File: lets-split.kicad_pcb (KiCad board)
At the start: 2 copper layers, 124 x 85.9 mm, 60 parts, among them J1 USB_C_Receptacle_USB2.0, SW1 Key_Tab, SW10 Key_D, SW11 Key_F, SW12 Key_G, SW13 Key_Shift, SW14 Key_Z, SW15 Key_X, SW16 Key_C, SW17 Key_V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

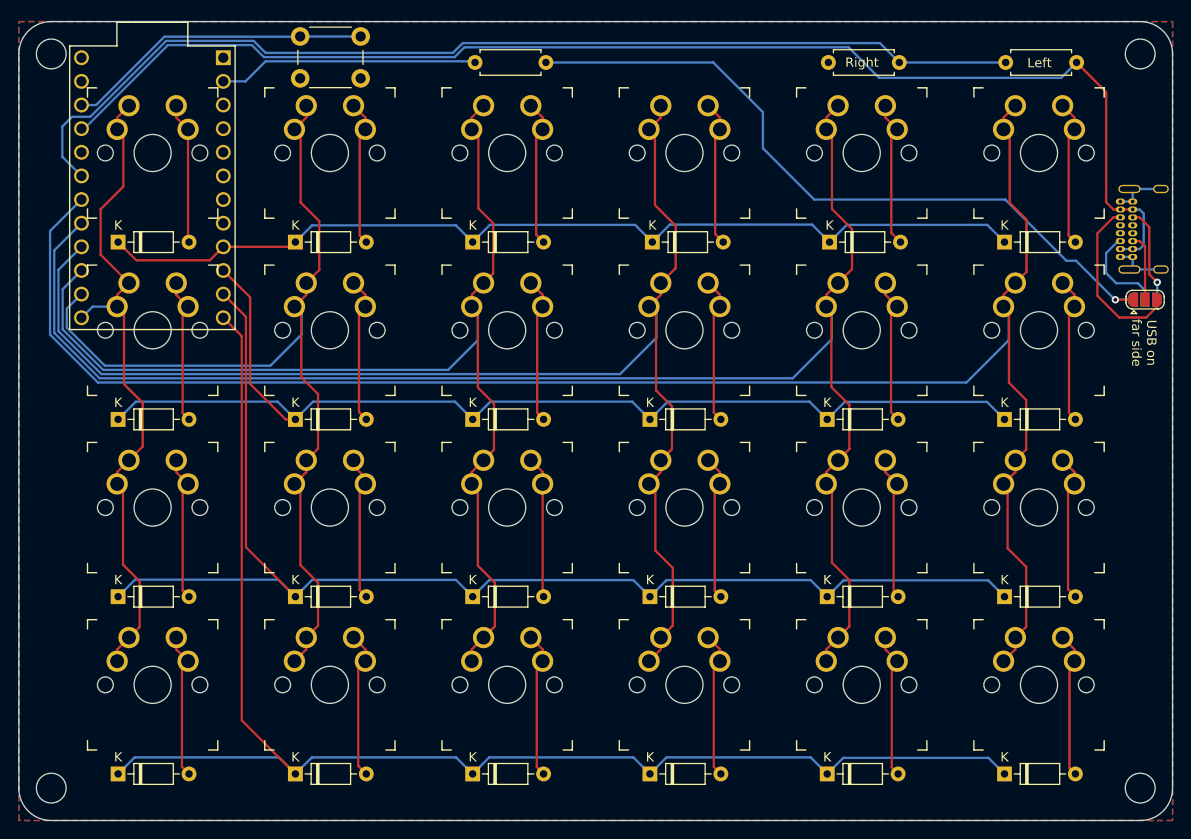
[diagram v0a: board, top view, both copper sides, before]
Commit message: Revised board
Moved controller over 1 column
moved usb-c to top edge
simplified routing overall

now only 1 via, and absolute minimum number of traces under the USB jack
(one each side!)
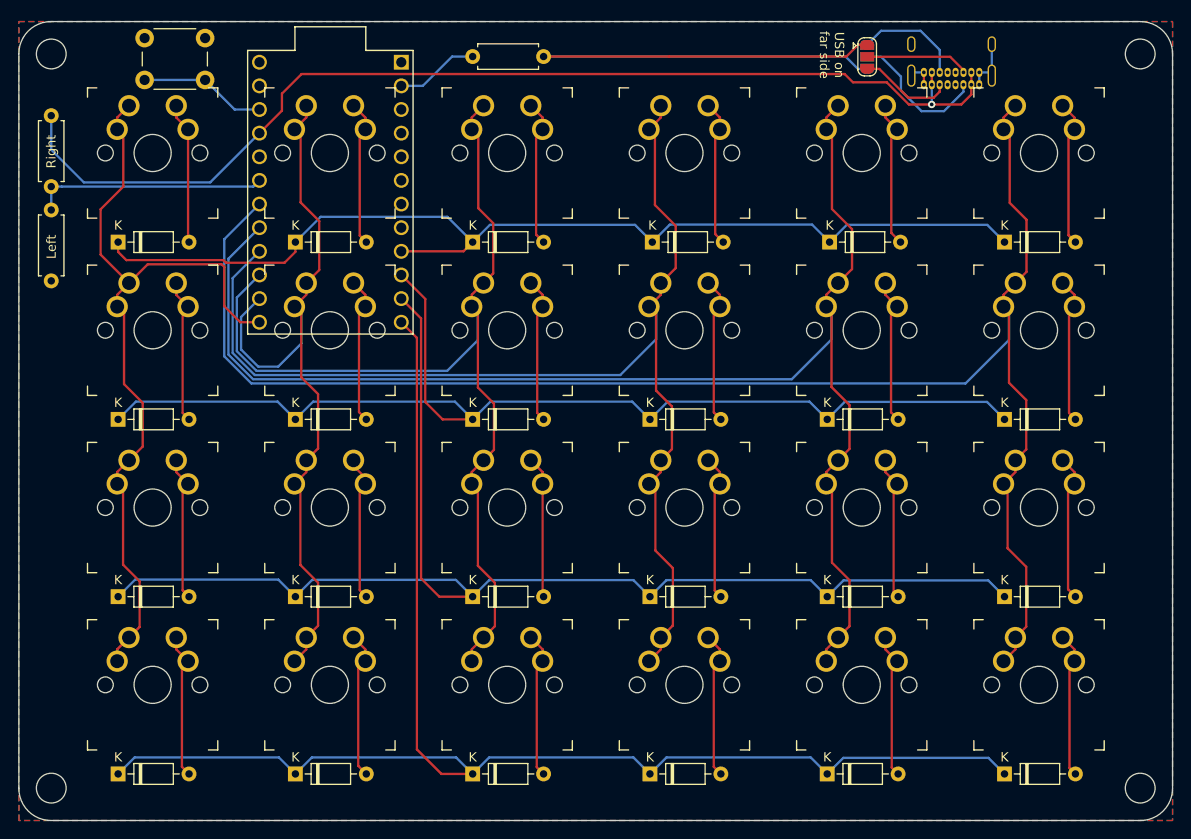
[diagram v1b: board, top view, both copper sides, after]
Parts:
- moved R1 103.4 mm to (79.2, 67.8), turned to 90 degrees
- moved R2 86.8 mm to (79.2, 78.0), turned to 90 degrees
- moved JP1 39.7 mm to (166.9, 53.9), turned to 270 degrees
- moved JP2 39.7 mm to (166.9, 53.9), turned to 270 degrees
- moved J1 32.5 mm to (175.9, 50.8), turned to 0 degrees
- moved U1 19.1 mm to (109.2, 68.4)
- moved SW25 11.2 mm to (95.7, 56.4), turned to 180 degrees
- moved R3 0.68 mm to (132.1, 53.8)
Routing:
- net HalfSelector: track 113.2 -> 25.2 mm
- net VCC: track 140.6 -> 117.5 mm, vias 0 -> 1
- net Serial1: track 28.7 -> 8.98 mm
- net Reset: track 33.1 -> 13.7 mm
- net Col5: track 170.7 -> 153.1 mm
- net Col3: track 125.0 -> 107.4 mm
- net Col6: track 193.1 -> 175.5 mm
- net Col4: track 148.3 -> 131.5 mm
- net Col2: track 103.4 -> 87.5 mm
- net Col1: track 72.0 -> 87.6 mm
- net Row1: track 103.0 -> 114.0 mm
- net Net-(J1-PadA5): track 18.5 -> 10.1 mm
- net Net-(JP1-Pad1): track 77.8 -> 70.6 mm, vias 1 -> 0
- net Net-(J1-PadA8): track 10.2 -> 15.3 mm
- net Net-(J1-PadB5): track 7.27 -> 11.2 mm
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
